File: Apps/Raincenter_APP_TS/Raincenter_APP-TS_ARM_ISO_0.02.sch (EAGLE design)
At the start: 26 parts

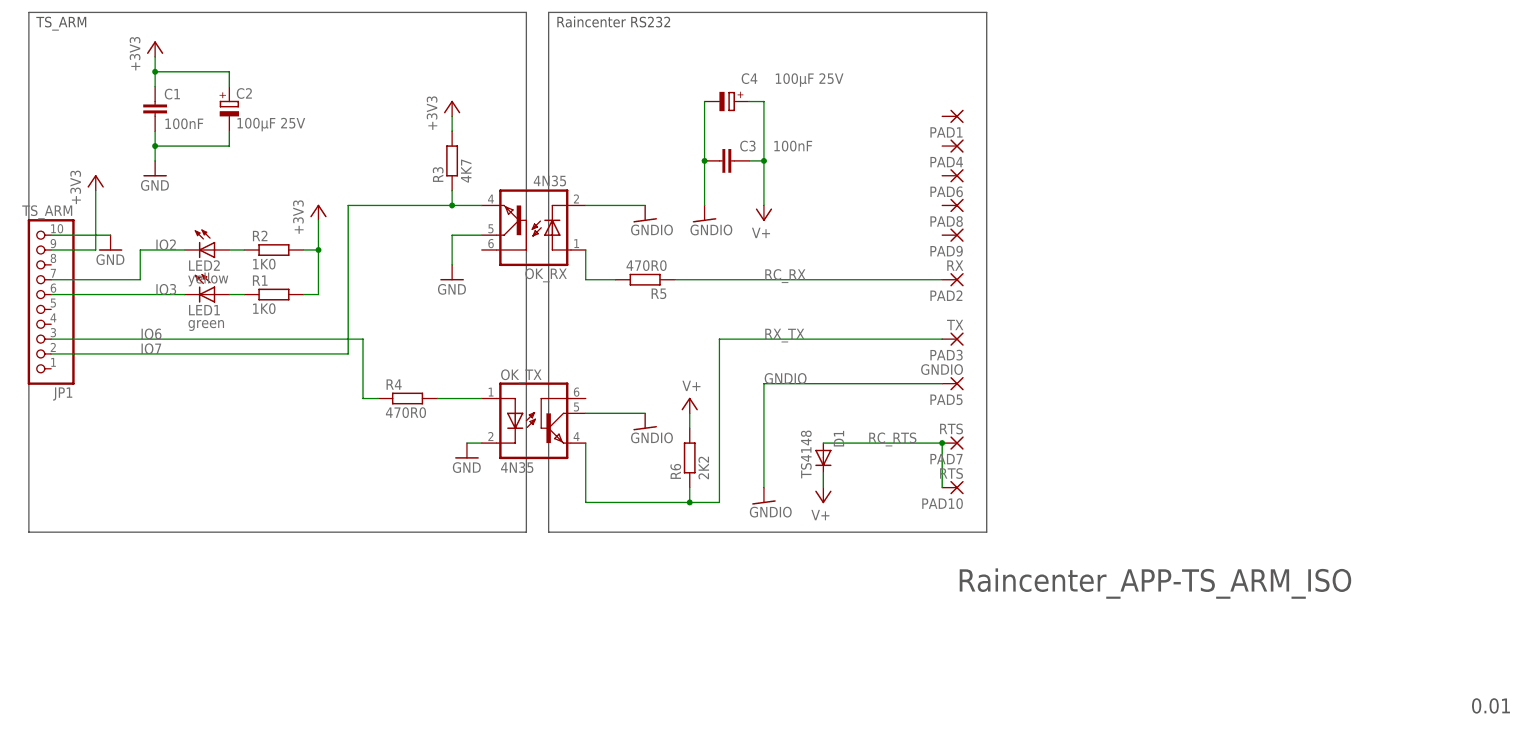
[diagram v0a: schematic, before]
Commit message: Raincenter_APP: fixed connected CTS instead of RTS, swapped Pin 4&5 of both optokopplers
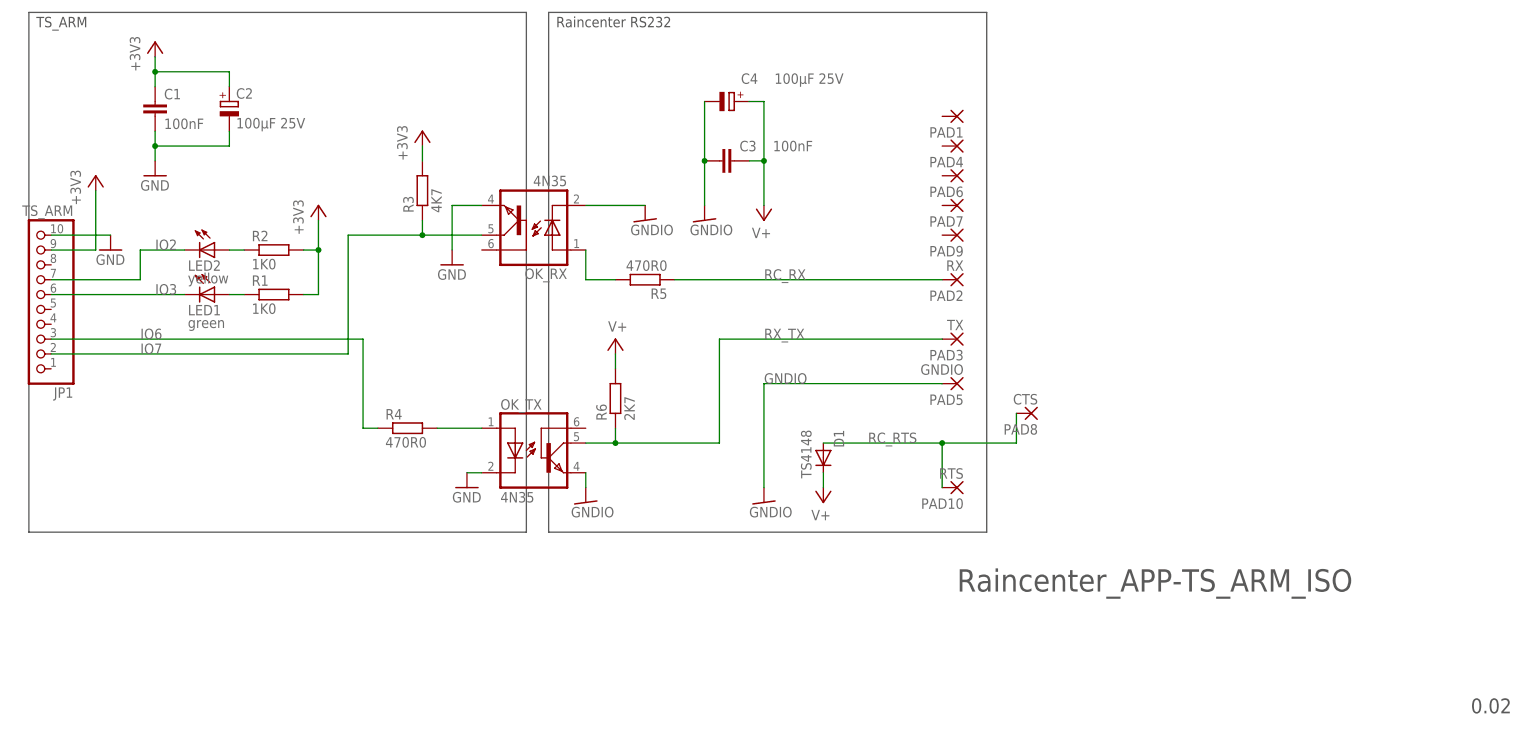
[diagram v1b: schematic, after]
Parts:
- PAD7: value RTS -> WIREPADSMD1,27-254
- PAD8: value WIREPADSMD1,27-254 -> CTS
- R6: value 2K2 -> 2K7
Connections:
- net GND: now also OK_RX.EMI; no longer OK_RX.COL
- net GNDIO: now also OK_TX.EMI; no longer OK_TX.COL
- net IO7: now also OK_RX.COL; no longer OK_RX.EMI
- net RC_RTS: now also PAD8.P; no longer PAD7.P
- net RX_TX: now also OK_TX.COL; no longer OK_TX.EMI
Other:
- note added: "0.02"
- note removed: "0.01"
- moved on the sheet: OK_TX, PAD7, PAD8, R3, R4, R6
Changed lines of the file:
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@@
 <attribute name="REICHELT" value="RND 1206 1 4,7K"/>
 </part>
-<part name="R6" library="rcl" deviceset="R-EU_" device="R1206" value="2K2">
+<part name="R6" library="rcl" deviceset="R-EU_" device="R1206" value="2K7">
 <attribute name="REICHELT" value="RND 1206 1 3,9K"/>
 </part>
@@
 <part name="PAD5" library="wirepad" deviceset="WIREPAD" device="SMD1,27-254" value="GNDIO"/>
 <part name="PAD6" library="wirepad" deviceset="WIREPAD" device="SMD1,27-254" value=""/>
-<part name="PAD7" library="wirepad" deviceset="WIREPAD" device="SMD1,27-254" value="RTS"/>
-<part name="PAD8" library="wirepad" deviceset="WIREPAD" device="SMD1,27-254" value=""/>
+<part name="PAD7" library="wirepad" deviceset="WIREPAD" device="SMD1,27-254" value=""/>
+<part name="PAD8" library="wirepad" deviceset="WIREPAD" device="SMD1,27-254" value="CTS"/>
 <part name="PAD9" library="wirepad" deviceset="WIREPAD" device="SMD1,27-254" value=""/>
 <part name="PAD10" library="wirepad" deviceset="WIREPAD" device="SMD1,27-254" value="RTS"/>
@@
 <plain>
 <text x="-45.72" y="-83.82" size="3.81" layer="97">Raincenter_APP-TS_ARM_ISO</text>
-<text x="42.164" y="-104.648" size="2.54" layer="97">0.01</text>
+<text x="42.164" y="-104.648" size="2.54" layer="97">0.02</text>
 <wire x1="-115.57" y1="-73.66" x2="-40.64" y2="-73.66" width="0.1524" layer="97"/>
 <wire x1="-40.64" y1="-73.66" x2="-40.64" y2="15.24" width="0.1524" layer="97"/>
@@
 </instance>
 <instance part="OK_RX" gate="G$1" x="-119.38" y="-22.86" rot="R180"/>
-<instance part="OK_TX" gate="G$1" x="-116.84" y="-53.34"/>
-<instance part="R4" gate="G$1" x="-139.7" y="-50.8">
-<attribute name="REICHELT" x="-139.7" y="-50.8" size="1.778" layer="96" display="off"/>
+<instance part="OK_TX" gate="G$1" x="-116.84" y="-58.42"/>
+<instance part="R4" gate="G$1" x="-139.7" y="-55.88">
+<attribute name="REICHELT" x="-139.7" y="-55.88" size="1.778" layer="96" display="off"/>
 </instance>
 <instance part="GND4" gate="G$1" x="-78.74" y="-68.58"/>
 <instance part="SUPPLY1" gate="1" x="-68.58" y="-68.58" rot="R180"/>
-<instance part="SUPPLY3" gate="1" x="-91.44" y="-50.8"/>
+<instance part="SUPPLY3" gate="1" x="-104.14" y="-40.64"/>
 <instance part="R5" gate="G$1" x="-99.06" y="-30.48" rot="R180">
 <attribute name="REICHELT" x="-99.06" y="-30.48" size="1.778" layer="96" rot="R180" display="off"/>
 </instance>
-<instance part="R3" gate="G$1" x="-132.08" y="-10.16" rot="R90">
-<attribute name="REICHELT" x="-132.08" y="-10.16" size="1.778" layer="96" rot="R90" display="off"/>
-</instance>
-<instance part="R6" gate="G$1" x="-91.44" y="-60.96" rot="R90">
-<attribute name="REICHELT" x="-91.44" y="-60.96" size="1.778" layer="96" rot="R90" display="off"/>
-</instance>
-<instance part="GND6" gate="1" x="-129.54" y="-60.96"/>
-<instance part="GND7" gate="G$1" x="-99.06" y="-55.88"/>
-<instance part="GND5" gate="1" x="-132.08" y="-30.48"/>
+<instance part="R3" gate="G$1" x="-137.16" y="-15.24" rot="R90">
+<attribute name="REICHELT" x="-137.16" y="-15.24" size="1.778" layer="96" rot="R90" display="off"/>
+</instance>
+<instance part="R6" gate="G$1" x="-104.14" y="-50.8" rot="R90">
+<attribute name="REICHELT" x="-104.14" y="-50.8" size="1.778" layer="96" rot="R90" display="off"/>
+</instance>
+<instance part="GND6" gate="1" x="-129.54" y="-66.04"/>
+<instance part="GND7" gate="G$1" x="-109.22" y="-68.58"/>
+<instance part="GND5" gate="1" x="-132.08" y="-27.94"/>
 <instance part="GND8" gate="G$1" x="-99.06" y="-20.32"/>
-<instance part="P+1" gate="G$1" x="-132.08" y="0"/>
+<instance part="P+1" gate="G$1" x="-137.16" y="-5.08"/>
 <instance part="C1" gate="G$1" x="-182.88" y="0"/>
 <instance part="C3" gate="G$1" x="-83.82" y="-10.16" smashed="yes" rot="R270">
@@
 <instance part="PAD5" gate="G$1" x="-45.72" y="-48.26" rot="R180"/>
 <instance part="PAD6" gate="G$1" x="-45.72" y="-12.7" rot="R180"/>
-<instance part="PAD7" gate="G$1" x="-45.72" y="-58.42" rot="R180"/>
-<instance part="PAD8" gate="G$1" x="-45.72" y="-17.78" rot="R180"/>
+<instance part="PAD7" gate="G$1" x="-45.72" y="-17.78" rot="R180"/>
+<instance part="PAD8" gate="G$1" x="-33.02" y="-53.34" rot="R180"/>
 <instance part="PAD9" gate="G$1" x="-45.72" y="-22.86" rot="R180"/>
 <instance part="PAD10" gate="G$1" x="-45.72" y="-66.04" rot="R180"/>
@@
 <pinref part="GND6" gate="1" pin="GND"/>
 <pinref part="OK_TX" gate="G$1" pin="C"/>
-<wire x1="-129.54" y1="-58.42" x2="-127" y2="-58.42" width="0.1524" layer="91"/>
-</segment>
-<segment>
+<wire x1="-129.54" y1="-63.5" x2="-127" y2="-63.5" width="0.1524" layer="91"/>
+</segment>
+<segment>
+<pinref part="OK_RX" gate="G$1" pin="EMI"/>
 <pinref part="GND5" gate="1" pin="GND"/>
-<pinref part="OK_RX" gate="G$1" pin="COL"/>
-<wire x1="-132.08" y1="-27.94" x2="-132.08" y2="-22.86" width="0.1524" layer="91"/>
-<wire x1="-132.08" y1="-22.86" x2="-127" y2="-22.86" width="0.1524" layer="91"/>
+<wire x1="-127" y1="-17.78" x2="-132.08" y2="-17.78" width="0.1524" layer="91"/>
+<wire x1="-132.08" y1="-17.78" x2="-132.08" y2="-25.4" width="0.1524" layer="91"/>
 </segment>
 </net>
@@
 <segment>
 <pinref part="R3" gate="G$1" pin="2"/>
-<wire x1="-132.08" y1="-5.08" x2="-132.08" y2="-2.54" width="0.1524" layer="91"/>
 <pinref part="P+1" gate="G$1" pin="+3V3"/>
+<wire x1="-137.16" y1="-7.62" x2="-137.16" y2="-10.16" width="0.1524" layer="91"/>
 </segment>
 </net>
@@
 <pinref part="R4" gate="G$1" pin="1"/>
 <label x="-185.42" y="-40.64" size="1.778" layer="95"/>
-<wire x1="-144.78" y1="-50.8" x2="-147.32" y2="-50.8" width="0.1524" layer="91"/>
-<wire x1="-147.32" y1="-50.8" x2="-147.32" y2="-40.64" width="0.1524" layer="91"/>
+<wire x1="-144.78" y1="-55.88" x2="-147.32" y2="-55.88" width="0.1524" layer="91"/>
+<wire x1="-147.32" y1="-55.88" x2="-147.32" y2="-40.64" width="0.1524" layer="91"/>
 <wire x1="-147.32" y1="-40.64" x2="-200.66" y2="-40.64" width="0.1524" layer="91"/>
 <pinref part="JP1" gate="A" pin="3"/>
@@
 <net name="IO7" class="0">
 <segment>
-<pinref part="OK_RX" gate="G$1" pin="EMI"/>
 <pinref part="R3" gate="G$1" pin="1"/>
-<wire x1="-127" y1="-17.78" x2="-132.08" y2="-17.78" width="0.1524" layer="91"/>
-<wire x1="-132.08" y1="-17.78" x2="-132.08" y2="-15.24" width="0.1524" layer="91"/>
-<junction x="-132.08" y="-17.78"/>
+<wire x1="-137.16" y1="-22.86" x2="-137.16" y2="-20.32" width="0.1524" layer="91"/>
 <label x="-185.42" y="-43.18" size="1.778" layer="95"/>
-<wire x1="-132.08" y1="-17.78" x2="-149.86" y2="-17.78" width="0.1524" layer="91"/>
-<wire x1="-149.86" y1="-17.78" x2="-149.86" y2="-43.18" width="0.1524" layer="91"/>
+<wire x1="-137.16" y1="-22.86" x2="-149.86" y2="-22.86" width="0.1524" layer="91"/>
+<wire x1="-149.86" y1="-22.86" x2="-149.86" y2="-43.18" width="0.1524" layer="91"/>
 <wire x1="-149.86" y1="-43.18" x2="-200.66" y2="-43.18" width="0.1524" layer="91"/>
 <pinref part="JP1" gate="A" pin="2"/>
+<pinref part="OK_RX" gate="G$1" pin="COL"/>
+<wire x1="-137.16" y1="-22.86" x2="-127" y2="-22.86" width="0.1524" layer="91"/>
+<junction x="-137.16" y="-22.86"/>
 </segment>
 </net>
 <net name="RX_TX" class="0">
 <segment>
-<wire x1="-91.44" y1="-68.58" x2="-86.36" y2="-68.58" width="0.1524" layer="91"/>
-<wire x1="-91.44" y1="-66.04" x2="-91.44" y2="-68.58" width="0.1524" layer="91"/>
+<wire x1="-104.14" y1="-58.42" x2="-86.36" y2="-58.42" width="0.1524" layer="91"/>
+<wire x1="-104.14" y1="-55.88" x2="-104.14" y2="-58.42" width="0.1524" layer="91"/>
 <pinref part="R6" gate="G$1" pin="1"/>
-<pinref part="OK_TX" gate="G$1" pin="EMI"/>
-<wire x1="-91.44" y1="-68.58" x2="-109.22" y2="-68.58" width="0.1524" layer="91"/>
-<wire x1="-109.22" y1="-68.58" x2="-109.22" y2="-58.42" width="0.1524" layer="91"/>
-<junction x="-91.44" y="-68.58"/>
-<wire x1="-86.36" y1="-68.58" x2="-86.36" y2="-40.64" width="0.1524" layer="91"/>
+<junction x="-104.14" y="-58.42"/>
+<wire x1="-86.36" y1="-58.42" x2="-86.36" y2="-40.64" width="0.1524" layer="91"/>
 <wire x1="-86.36" y1="-40.64" x2="-48.26" y2="-40.64" width="0.1524" layer="91"/>
 <label x="-78.74" y="-40.64" size="1.778" layer="95"/>
 <pinref part="PAD3" gate="G$1" pin="P"/>
+<pinref part="OK_TX" gate="G$1" pin="COL"/>
+<wire x1="-104.14" y1="-58.42" x2="-109.22" y2="-58.42" width="0.1524" layer="91"/>
 </segment>
 </net>
@@
 <label x="-78.74" y="-48.26" size="1.778" layer="95"/>
 <pinref part="PAD5" gate="G$1" pin="P"/>
-</segment>
-<segment>
-<pinref part="OK_TX" gate="G$1" pin="COL"/>
-<pinref part="GND7" gate="G$1" pin="GNDIO"/>
-<wire x1="-109.22" y1="-53.34" x2="-99.06" y2="-53.34" width="0.1524" layer="91"/>
 </segment>
 <segment>
@@
 <junction x="-88.9" y="-10.16"/>
 </segment>
+<segment>
+<pinref part="GND7" gate="G$1" pin="GNDIO"/>
+<pinref part="OK_TX" gate="G$1" pin="EMI"/>
+<wire x1="-109.22" y1="-66.04" x2="-109.22" y2="-63.5" width="0.1524" layer="91"/>
+</segment>
 </net>
 <net name="V+" class="0">
@@
 <pinref part="R6" gate="G$1" pin="2"/>
 <pinref part="SUPPLY3" gate="1" pin="V+"/>
-<wire x1="-91.44" y1="-55.88" x2="-91.44" y2="-53.34" width="0.1524" layer="91"/>
+<wire x1="-104.14" y1="-45.72" x2="-104.14" y2="-43.18" width="0.1524" layer="91"/>
 </segment>
 <segment>
@@
 <pinref part="R4" gate="G$1" pin="2"/>
 <pinref part="OK_TX" gate="G$1" pin="A"/>
-<wire x1="-134.62" y1="-50.8" x2="-127" y2="-50.8" width="0.1524" layer="91"/>
+<wire x1="-134.62" y1="-55.88" x2="-127" y2="-55.88" width="0.1524" layer="91"/>
 </segment>
 </net>
@@
 <label x="-60.96" y="-58.42" size="1.778" layer="95"/>
 <pinref part="D1" gate="G$1" pin="A"/>
-<pinref part="PAD7" gate="G$1" pin="P"/>
 <pinref part="PAD10" gate="G$1" pin="P"/>
-<wire x1="-48.26" y1="-58.42" x2="-48.26" y2="-66.04" width="0.1524" layer="91"/>
+<pinref part="PAD8" gate="G$1" pin="P"/>
+<wire x1="-48.26" y1="-66.04" x2="-48.26" y2="-58.42" width="0.1524" layer="91"/>
 <junction x="-48.26" y="-58.42"/>
-</segment>
-</net>
+<wire x1="-48.26" y1="-58.42" x2="-35.56" y2="-58.42" width="0.1524" layer="91"/>
+<wire x1="-35.56" y1="-58.42" x2="-35.56" y2="-53.34" width="0.1524" layer="91"/>
+</segment>
+</net>
